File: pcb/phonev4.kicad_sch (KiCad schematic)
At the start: 37 parts, among them J1 coin, J2 keypad, J3 display, J4 RJ9, J5 mic, J6 card_reader, J7 speaker, Q1 Si2319CDS, U2 TDA2822M

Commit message: pcb: Move D2 ESD protection from coin_rx to speaker_front+
- D2 (PRTR5V0U2X) now protects speaker_front+ (TDA2822 ringer output)
  instead of coin_rx; coin validator control board isolates serial
- D1 protects mic+ and speaker_receiver+ on J4; D2 I/O2 left unconnected
- Add SCHEMATIC_D2_CHANGES.md with implementation notes and I/O2 options
- Update README, BOM, AUDIT to match

Co-authored-by: Cursor <cursoragent@cursor.com>
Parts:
- F1: footprint Fuse:Fuse_Radial_D10.0mm_P5.00mm -> Capacitor_THT:CP_Radial_D10.0mm_P5.00mm
- renumbered C-arduino1 to C1, C_inB to C10, C_outA to C11, C_outB to C12, C-arduino-display1 to C2, C-card1 to C3, C-coin1 to C4, C-raspi1 to C5, C_dec to C6, C_vcc to C7, C_ripple to C8, C_inA to C9
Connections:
- net card_seated is gone; now on net mag_cls: J6.12 (Pin_12)
- net 5V_MAIN: now also C6.2, C7.2, U2.6 (V+)
- net coin_rx: no longer D2.2 (I/O1)
- net speaker_front+: now also D2.2 (I/O1)
- net BOOST_IN+: now reaches Q1.3 (D), U1.1 (IN+)
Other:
- moved on the sheet: F1, Q1

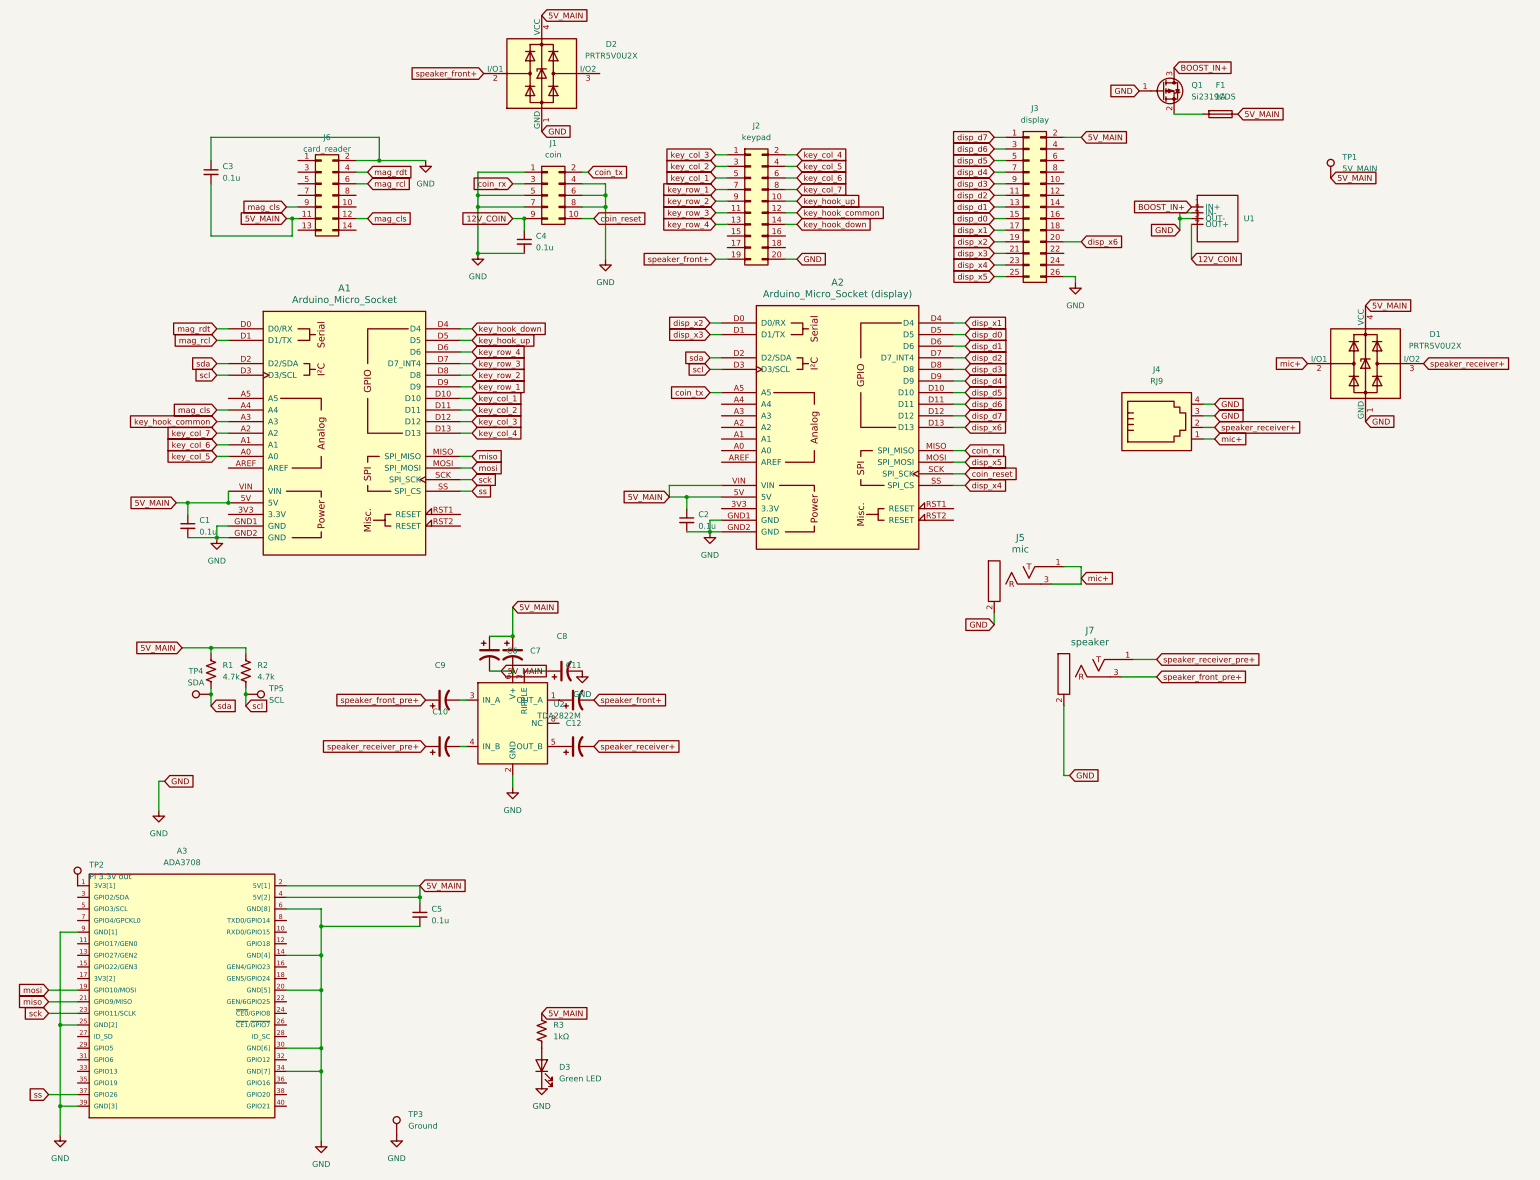
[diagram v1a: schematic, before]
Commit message: pcb: diode reannotation, ERC fixes, no-connect markers
- Update docs for D1-D3 (P6KE6.8CA TVS), D4 (power LED)
- Add PWR_FLAGs for 5V_MAIN, GND, 3.3V nets
- Fix C6/C7 bypass wiring (parallel to GND, not series)
- Add no_connect markers for 59 intentionally unused pins
- Remove dangling wires at 288.29mm and 110.49/130.81
- Add add_no_connect.py script for future ERC sync
- Add F1 fuse footprint, fp-lib-table, DESIGN_OPTIONS

Co-authored-by: Cursor <cursoragent@cursor.com>
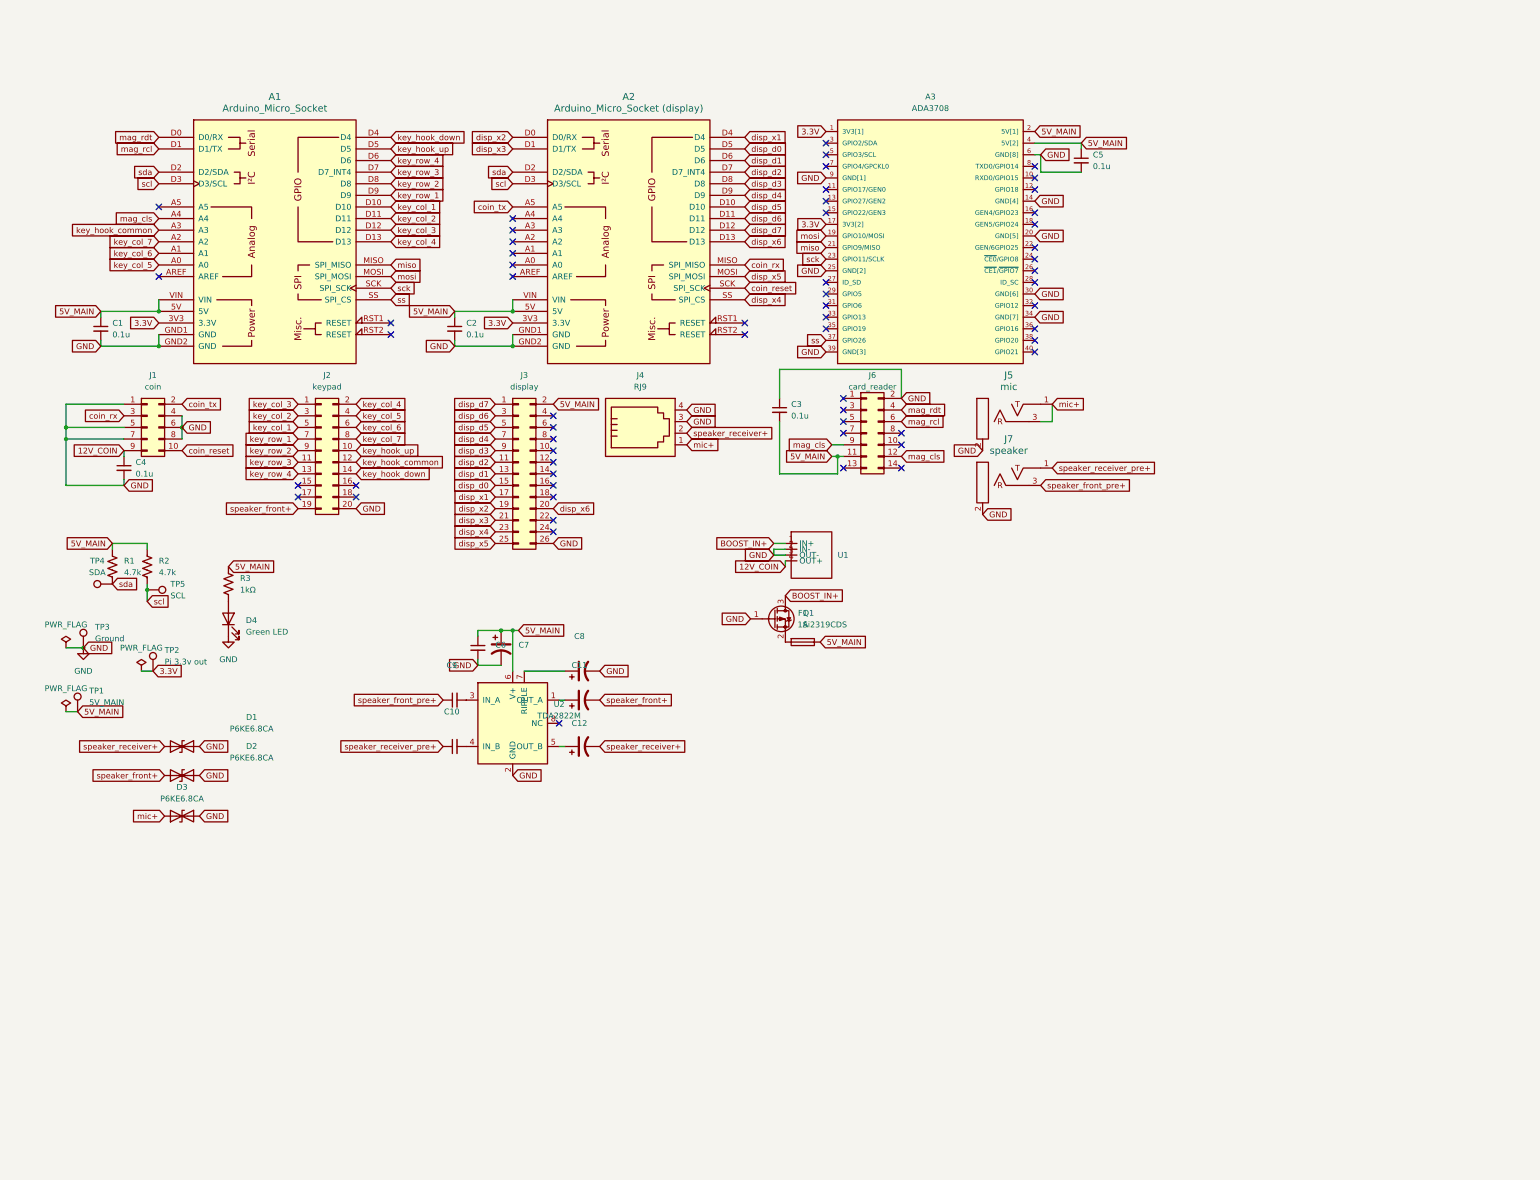
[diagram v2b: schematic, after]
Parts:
- removed D1: PRTR5V0U2X, Package_TO_SOT_SMD:SOT-143, symbol Power_Protection:PRTR5V0U2X
- added D1, D3: P6KE6.8CA, Diode_THT:D_DO-15_P10.16mm_Horizontal, symbol phone:P6KE6.8CA
- C10, C6, C9: symbol PCM_Capacitor_US_AKL:CP_Axial_L18.0mm_D10.0mm_P25.00mm -> Device:C_Small
- D2: value PRTR5V0U2X -> P6KE6.8CA; footprint Package_TO_SOT_SMD:SOT-143 -> Diode_THT:D_DO-15_P10.16mm_Horizontal; symbol Power_Protection:PRTR5V0U2X -> phone:P6KE6.8CA
- F1: footprint Capacitor_THT:CP_Radial_D10.0mm_P5.00mm -> footprints:Fuse_Radial_D10.0mm_P5.00mm
- renumbered D3 to D4
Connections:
- net 5V_MAIN: no longer C6.2, C7.2, D2.4 (VCC)
- net GND: now also C6.2, C7.2, D2.2, D1.2, D3.2; no longer D2.1 (GND)
- net mic+: now also D3.1
- net speaker_front+: now also D2.1; no longer D2.2 (I/O1)
- net speaker_receiver+: now also D1.1
- net 3.3V: now reaches A3.1 (3V3[1]), TP2.1
- net 3.3V: now also A1.3V3 (3.3V), A2.3V3 (3.3V), A3.17 (3V3[2])
- no-connect marks 0 -> 59
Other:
- moved on the sheet: A1, A2, A3, C1, C11, C12, C2, C3, C4, C5, C7, C8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
